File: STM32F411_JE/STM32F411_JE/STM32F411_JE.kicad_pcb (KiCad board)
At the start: 2 copper layers, 63.5 x 27.5 mm, 32 parts, among them J1 USB4105-GF-A, J2 Screw_Terminal_01x04, J3 Conn_01x20_Socket, J4 Conn_01x20_Socket, U1 STM32F411CEU6, U2 AP7343, Y1 25 Mhz

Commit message: Se agregan etiquetas de los pines al diseño de la PCB
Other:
- board text added: "3.3V"
- board text added: "5V"
- board text added: "A0"
- board text added: "A1"
- board text added: "A10"
- board text added: "A11"
- board text added: "A12"
- board text added: "A15"
- board text added: "A2"
- board text added: "A3"
- board text added: "A4"
- board text added: "A5"
- board text added: "A6"
- board text added: "A7"
- board text added: "A8"
- board text added: "A9"
- board text added: "B0"
- board text added: "B1"
- board text added: "B10"
- board text added: "B12"
- board text added: "B13"
- board text added: "B14"
- board text added: "B15"
- board text added: "B2"
- board text added: "B3"
- board text added: "B4"
- board text added: "B5"
- board text added: "B6"
- board text added: "B7"
- board text added: "B8"
- board text added: "B9"
- board text added: "C13"
- board text added: "C14"
- board text added: "C15"
- board text added: "GND"
- board text added: "NRST"
- board text added: "SWCLK"
- board text added: "SWDIO"
- board text added: "VB"

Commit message: diseño pcb
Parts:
- moved C2 4.53 mm to (66.5, 35.0), turned to 0 degrees
- moved D1 1.06 mm to (81.0, 23.9)
- moved C12 1.00 mm to (75.0, 27.0)
- moved C7 1.00 mm to (57.5, 35.0)
- moved D3 1.00 mm to (81.0, 31.0)
- moved R3 1.00 mm to (42.0, 21.5)
- moved C11 0.50 mm to (40.0, 25.0)
- moved C8 0.50 mm to (69.5, 23.0)
- moved D2 0.50 mm to (75.0, 21.0)
- moved R5 0.50 mm to (33.0, 34.5)
- moved R6 0.50 mm to (33.0, 20.5)
- moved Y1 0.50 mm to (75.0, 32.5)
- moved J4 0.08 mm to (36.5, 40.0)
- turned U1 to 135 degrees
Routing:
- net /3.3V: track 0.00 -> 164.0 mm, vias 0 -> 1
- net /5V: track 0.00 -> 94.6 mm, vias 0 -> 2
- net /VB: track 0.00 -> 76.8 mm
- net /NRST: track 0.00 -> 74.8 mm, vias 0 -> 3
- net /PB13: track 0.00 -> 61.3 mm, vias 0 -> 1
- net /PB12: track 0.00 -> 53.8 mm, vias 0 -> 1
- net Net-(C9-Pad2): track 0.00 -> 50.6 mm, vias 0 -> 2
- net /PC15: track 0.00 -> 48.2 mm, vias 0 -> 1
- net /PC14: track 0.00 -> 47.5 mm, vias 0 -> 3
- net /PA12: track 0.00 -> 44.5 mm, vias 0 -> 1
- net /PA13: track 0.00 -> 43.2 mm, vias 0 -> 1
- net /PA0: track 0.00 -> 41.9 mm, vias 0 -> 1
- net /PA11: track 0.00 -> 39.8 mm, vias 0 -> 1
- net /PA14: track 0.00 -> 39.1 mm, vias 0 -> 2
- net /PC13: track 0.00 -> 33.3 mm, vias 0 -> 1
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- added copper zone on B.Cu, net GND
- added copper zone on F.Cu, net GND

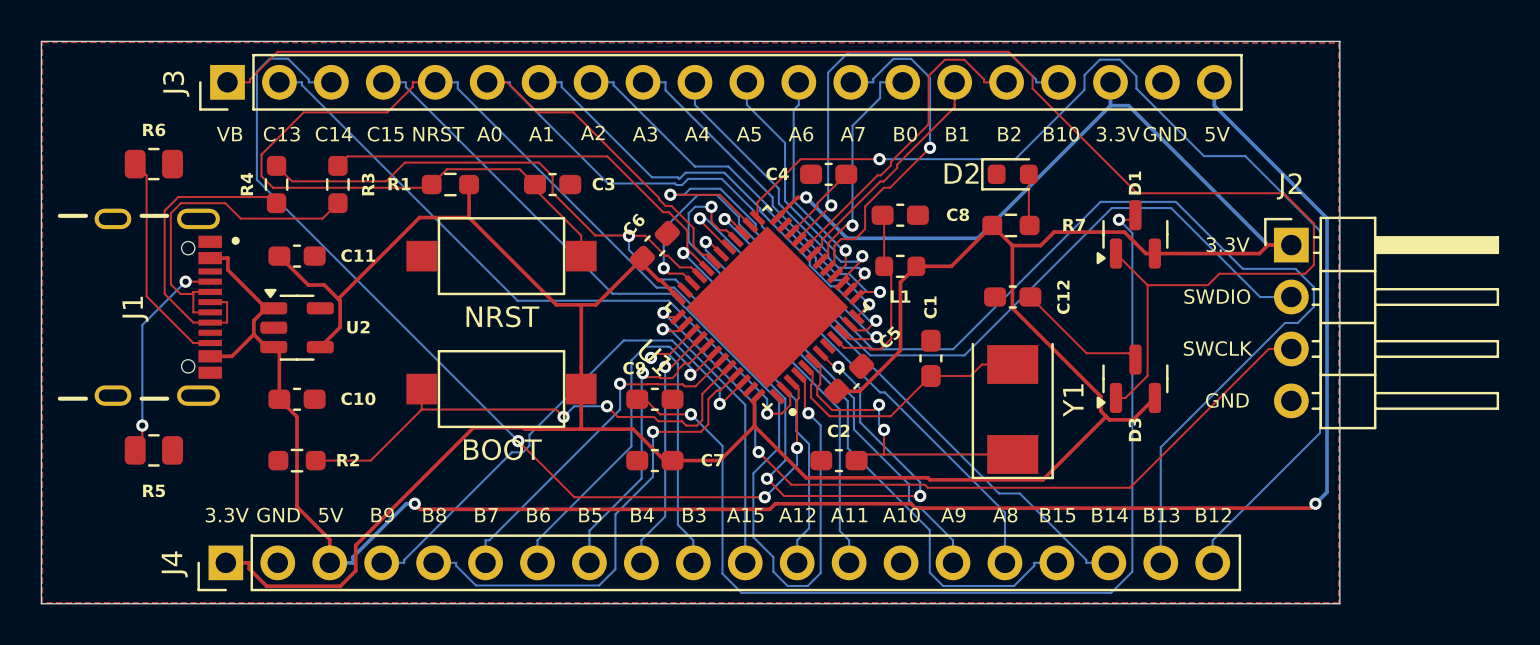
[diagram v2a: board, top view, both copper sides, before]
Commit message: Se termina el diseño de la zona de cobre de la pcb
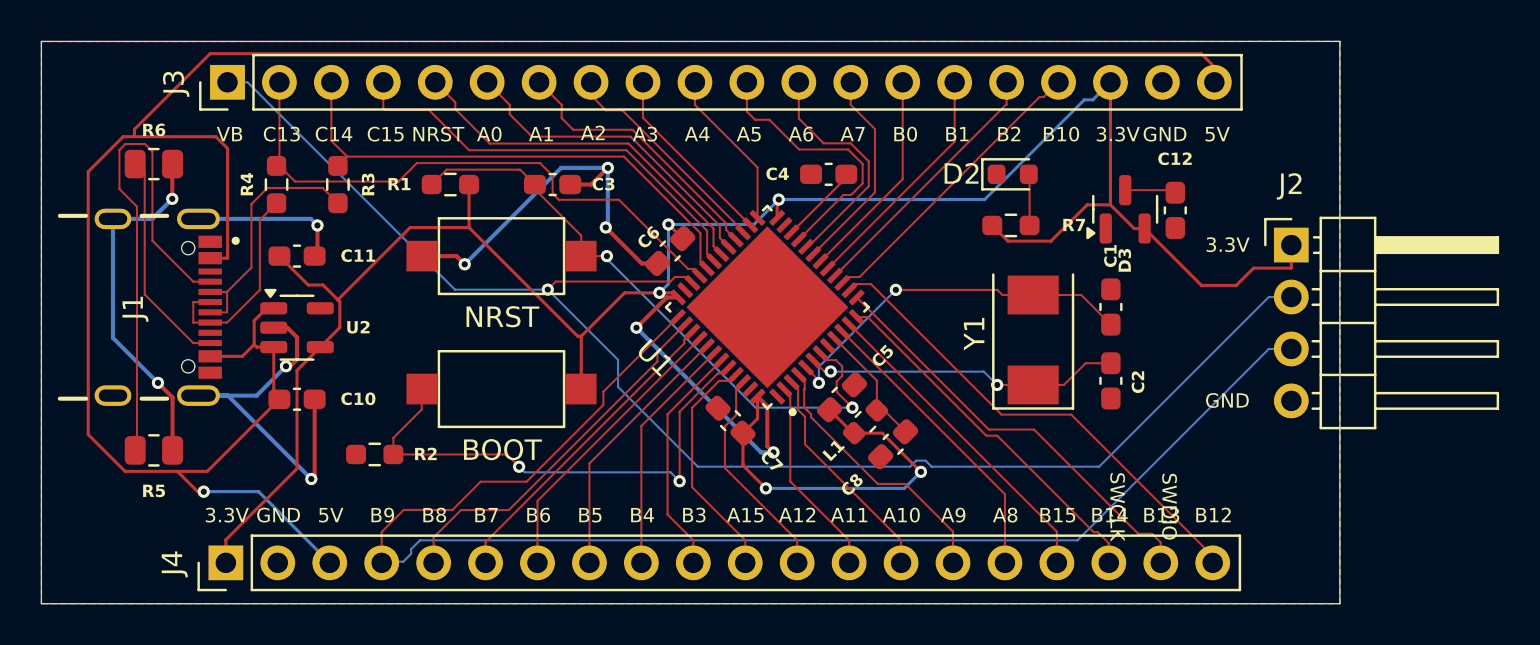
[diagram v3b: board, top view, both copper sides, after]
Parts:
- removed C9: 100nF, Capacitor_SMD:C_0603_1608Metric_Pad1.08x0.95mm_HandSolder
- removed D1: BAT54C, Package_TO_SOT_SMD:SOT-23
- moved C2 13.9 mm to (79.8, 31.1), turned to 90 degrees
- moved C8 11.2 mm to (69.2, 34.2), turned to -135 degrees
- moved C1 9.15 mm to (79.8, 27.5)
- moved C12 9.01 mm to (83.0, 22.8), turned to 90 degrees
- moved D3 8.30 mm to (80.5, 22.7)
- moved L1 7.79 mm to (67.8, 33.1), turned to -135 degrees
- moved C7 4.18 mm to (61.2, 33.0), turned to 135 degrees
- moved R2 3.81 mm to (43.8, 34.7)
- moved Y1 3.54 mm to (76.0, 29.1)
- moved C5 0.97 mm to (66.7, 31.9)
- moved C6 0.79 mm to (58.2, 24.8), turned to -135 degrees
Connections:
- C10 pad 2: unconnected-(C10-Pad2) -> GND
- J3 pad 1: /VB -> /PA13
- J3 pad 10: /PA4 -> /PB12
- J3 pad 11: /PA5 -> /PB10
- J3 pad 12: /PA6 -> /PB2
- J3 pad 13: /PA7 -> /PB1
- J3 pad 15: /PB1 -> /PA7
- J3 pad 16: /PB2 -> /PA6
- J3 pad 17: /PB10 -> /PA5
- J3 pad 2: /PC13 -> /PA12
- J3 pad 3: /PC14 -> /PA11
- J3 pad 4: /PC15 -> /PA10
- J3 pad 5: /NRST -> /PA9
- J3 pad 6: /PA0 -> /PA8
- J3 pad 7: /PA1 -> /PB15
- J3 pad 8: /PA2 -> /PB14
- J3 pad 9: /PA3 -> /PB13
- J4 pad 10: /PB3 -> /PB7
- J4 pad 11: /PA15 -> /PB8
- J4 pad 12: /PA12 -> /PB9
- J4 pad 13: /PA11 -> /PC13
- J4 pad 14: /PA10 -> /PC14
- J4 pad 15: /PA9 -> /PC15
- J4 pad 16: /PA8 -> /PA0
- J4 pad 17: /PB15 -> /PA1
- J4 pad 18: /PB14 -> /PA2
- J4 pad 19: /PB13 -> /PA3
- J4 pad 20: /PB12 -> /PA4
- J4 pad 4: /PB9 -> /PA14
- J4 pad 5: /PB8 -> /PA15
- J4 pad 6: /PB7 -> /PB3
- J4 pad 7: /PB6 -> /PB4
- J4 pad 9: /PB4 -> /PB6
- U1 pad 31: /PA0 -> /PA10
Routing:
- net /VB: track 76.8 -> 0.00 mm
- net GND: track 0.00 -> 63.8 mm, vias 0 -> 8
- net /PB13: track 61.3 -> 9.16 mm, vias 1 -> 0
- net Net-(C9-Pad2): track 50.6 -> 0.00 mm, vias 2 -> 0
- net /PB12: track 53.8 -> 7.90 mm, vias 1 -> 0
- net /NRST: track 74.8 -> 30.3 mm, vias 3 -> 2
- net /PC14: track 47.5 -> 11.1 mm, vias 3 -> 0
- net /PC15: track 48.2 -> 13.1 mm, vias 1 -> 0
- net /PA14: track 39.1 -> 69.7 mm, vias 2 -> 0
- net /3.3V: track 164.0 -> 133.4 mm, vias 1 -> 7
- net /PA13: track 43.2 -> 71.7 mm
- net /PA0: track 41.9 -> 14.6 mm, vias 1 -> 0
- net /PC13: track 33.3 -> 9.79 mm, vias 1 -> 0
- net /PA10: track 0.00 -> 21.2 mm
- net /PB15: track 33.0 -> 13.4 mm, vias 1 -> 0
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- removed copper zone on B.Cu, net GND

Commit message: se añadio logo
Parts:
- added G***: LOGO, images:logo, F.Cu at (30.6, 38.4)
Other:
- board text added: "JE MECHATRONICS"

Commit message: fixing
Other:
- board text added: "A13"
- board text added: "A14"
- board text removed: "A6"
- board text removed: "NRST"
- board text removed: "VB"
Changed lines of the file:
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@@
 		(tags "capacitor handsolder")
 		(property "Reference" "C1"
-			(at -2.5 0 90)
+			(at 0.0125 -1.225 90)
 			(layer "F.SilkS")
 			(effects
@@
 		(tags "SOT TO_SOT_SMD")
 		(property "Reference" "D3"
-			(at -2.5 0 90)
+			(at 2.3875 0.25 180)
 			(layer "F.SilkS")
 			(effects
@@
 		(layer "Edge.Cuts")
 	)
-	(gr_text "B15\n"
+	(gr_text "A1\n"
 		(at 77.2 38.1 0)
 		(layer "F.SilkS")
@@
 		)
 	)
-	(gr_text "B3"
+	(gr_text "B7"
 		(at 59.42 38.1 0)
 		(layer "F.SilkS")
@@
 	)
 	(gr_text "GND\n"
-		(at 82.45 19.47 0)
+		(at 82.51 19.39 0)
 		(layer "F.SilkS")
 		(effects
@@
 	)
 	(gr_text "3.3V\n"
-		(at 80.13 19.47 0)
+		(at 79.95 19.4 0)
 		(layer "F.SilkS")
 		(effects
@@
 	)
 	(gr_text "SWDIO"
-		(at 82.235 37.25 -90)
+		(at 85.01 27.48 0)
 		(layer "F.SilkS")
 		(effects
@@
 		)
 	)
-	(gr_text "B4"
+	(gr_text "B6"
 		(at 56.88 38.1 0)
 		(layer "F.SilkS")
@@
 		)
 	)
-	(gr_text "A8"
+	(gr_text "A0"
 		(at 74.66 38.1 0)
 		(layer "F.SilkS")
@@
 		)
 	)
-	(gr_text "B12\n"
+	(gr_text "A4"
 		(at 84.82 38.1 0)
 		(layer "F.SilkS")
@@
 		)
 	)
-	(gr_text "A7\n"
+	(gr_text "B1"
 		(at 67.21 19.47 0)
 		(layer "F.SilkS")
@@
 		)
 	)
-	(gr_text "A1"
+	(gr_text "B15"
 		(at 51.97 19.47 0)
 		(layer "F.SilkS")
@@
 		)
 	)
-	(gr_text "A5\n"
+	(gr_text "B10\n"
 		(at 62.13 19.47 0)
 		(layer "F.SilkS")
@@
 		)
 	)
-	(gr_text "C15\n"
+	(gr_text "A10\n"
 		(at 44.35 19.47 0)
 		(layer "F.SilkS")
@@
 		)
 	)
-	(gr_text "NRST\n"
+	(gr_text "A9"
 		(at 46.89 19.47 0)
 		(layer "F.SilkS")
@@
 	)
 	(gr_text "SWCLK"
-		(at 79.695 37.25 -90)
+		(at 84.96 29.97 0)
 		(layer "F.SilkS")
 		(effects
@@
 		)
 	)
-	(gr_text "B9"
+	(gr_text "A14"
 		(at 44.18 38.1 0)
 		(layer "F.SilkS")
@@
 		)
 	)
-	(gr_text "B13\n"
+	(gr_text "A3"
 		(at 82.28 38.1 0)
 		(layer "F.SilkS")
@@
 		)
 	)
-	(gr_text "B1\n"
+	(gr_text "A7\n"
 		(at 72.29 19.47 0)
 		(layer "F.SilkS")
@@
 		)
 	)
-	(gr_text "B14\n"
+	(gr_text "A2"
 		(at 79.74 38.1 0)
 		(layer "F.SilkS")
@@
 		)
 	)
-	(gr_text "A3\n"
+	(gr_text "B13"
 		(at 57.05 19.47 0)
 		(layer "F.SilkS")
@@
 		)
 	)
-	(gr_text "B7"
+	(gr_text "B3"
 		(at 49.26 38.1 0)
 		(layer "F.SilkS")
@@
 		)
 	)
-	(gr_text "A11"
+	(gr_text "C13"
 		(at 67.04 38.1 0)
 		(layer "F.SilkS")
@@
 	)
 	(gr_text "5V"
-		(at 84.99 19.47 0)
+		(at 84.99 19.35 0)
 		(layer "F.SilkS")
 		(effects
@@
 		)
 	)
-	(gr_text "C13\n"
+	(gr_text "A12"
 		(at 39.27 19.47 0)
 		(layer "F.SilkS")
@@
 		)
 	)
-	(gr_text "VB"
+	(gr_text "A13"
 		(at 36.73 19.47 0)
 		(layer "F.SilkS")
@@
 		)
 	)
-	(gr_text "B10\n"
+	(gr_text "A5"
 		(at 77.37 19.47 0)
 		(layer "F.SilkS")
@@
 		)
 	)
-	(gr_text "A12"
+	(gr_text "B9\n"
 		(at 64.5 38.1 0)
 		(layer "F.SilkS")
@@
 		)
 	)
-	(gr_text "A2"
+	(gr_text "B14\n"
 		(at 54.51 19.41412 0)
 		(layer "F.SilkS")
@@
 		)
 	)
-	(gr_text "C14"
+	(gr_text "A11\n"
 		(at 41.81 19.47 0)
 		(layer "F.SilkS")
@@
 		)
 	)
-	(gr_text "B8"
+	(gr_text "A15"
 		(at 46.72 38.1 0)
 		(layer "F.SilkS")
@@
 		)
 	)
-	(gr_text "B6"
+	(gr_text "B4"
 		(at 51.8 38.1 0)
 		(layer "F.SilkS")
@@
 		)
 	)
-	(gr_text "A4\n"
+	(gr_text "B12\n"
 		(at 59.59 19.47 0)
 		(layer "F.SilkS")
@@
 		)
 	)
-	(gr_text "A6\n"
+	(gr_text "B2"
 		(at 64.67 19.47 0)
 		(layer "F.SilkS")
@@
 		)
 	)
-	(gr_text "A10"
+	(gr_text "C14"
 		(at 69.58 38.1 0)
 		(layer "F.SilkS")
@@
 		)
 	)
-	(gr_text "A15"
+	(gr_text "B8"
 		(at 61.96 38.1 0)
 		(layer "F.SilkS")
@@
 		)
 	)
-	(gr_text "A9"
+	(gr_text "C15"
 		(at 72.12 38.1 0)
 		(layer "F.SilkS")
@@
 		)
 	)
-	(gr_text "A0\n"
+	(gr_text "A8\n"
 		(at 49.43 19.47 0)
 		(layer "F.SilkS")
